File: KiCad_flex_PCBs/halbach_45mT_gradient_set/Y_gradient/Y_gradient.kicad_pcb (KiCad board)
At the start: 2 copper layers, 217.6 x 125.7 mm, 70 parts, among them J1- SolderPad, J2+ SolderPad

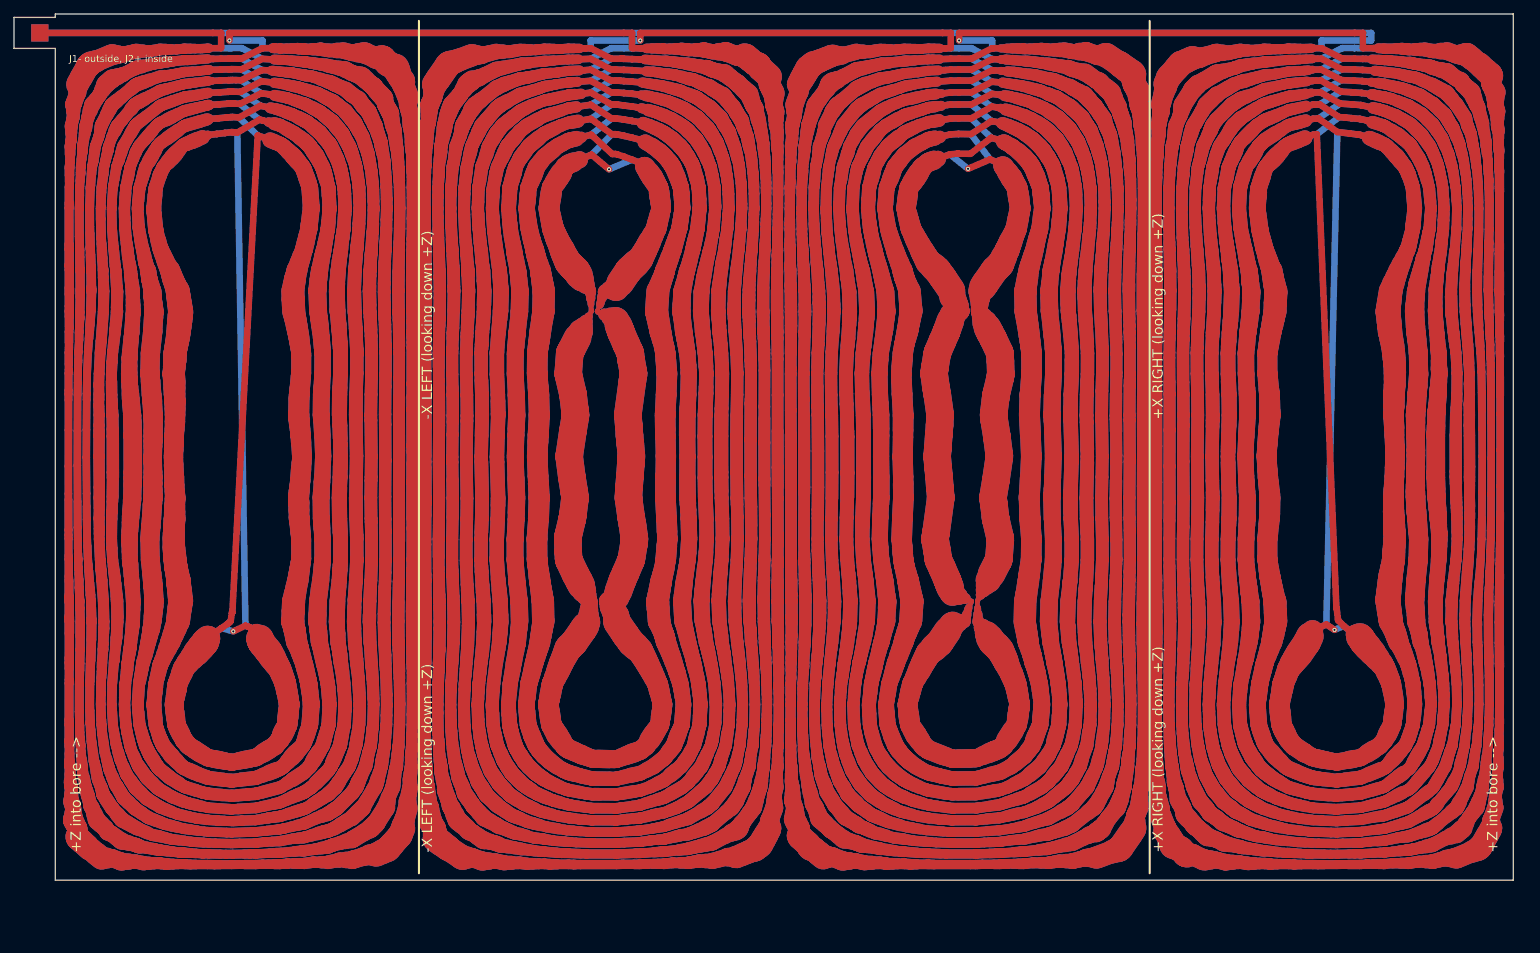
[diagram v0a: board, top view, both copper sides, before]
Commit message: Move the feed tab to the end edge of the flex PCBs
The J1/J2 tab now sticks out past the +axial end of the coil instead of
out of the seam, so the rolled seam is clean and there is room to solder
the leads. Feed and return run as a stacked F.Cu/B.Cu pair along the seam
edge to the routing channel. Larger pads (3 mm) on a 10 mm tab. The tabs
of the three coils sit at their seams: 12, 1 and 6 o'clock looking down +Z.
All boards: DRC clean, same-net gap >= 0.15 mm, re-simulation unchanged.

Co-Authored-By: Claude Opus 5.5 <noreply@anthropic.com>
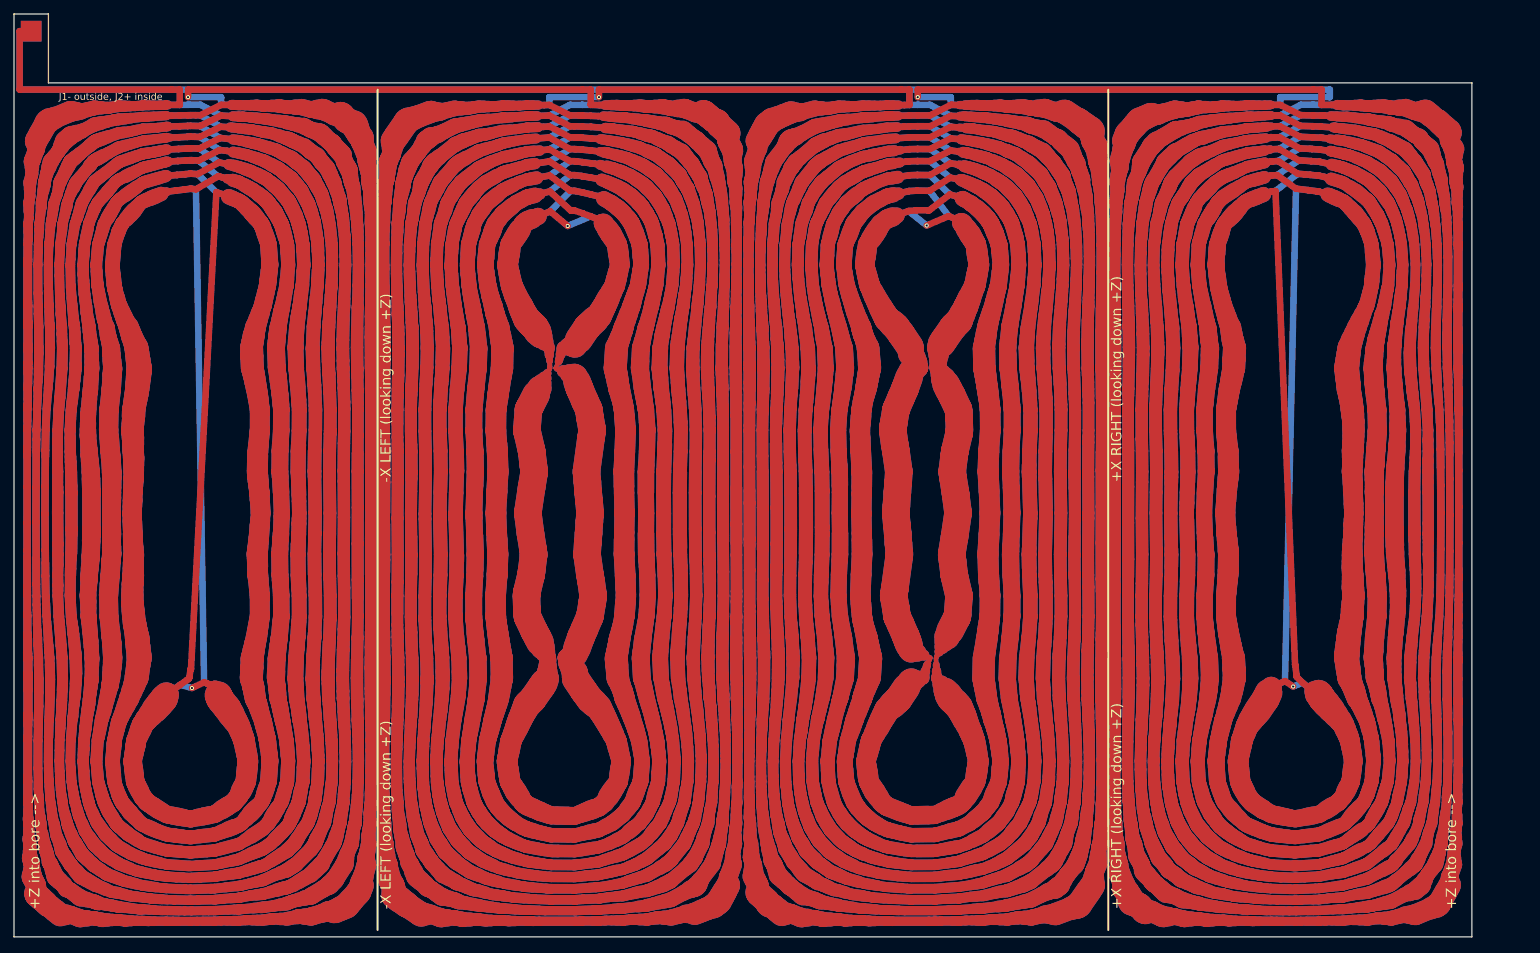
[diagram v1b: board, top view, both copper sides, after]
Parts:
- moved NT9 10.2 mm to (35.1, 106.7)
- moved NT1 10.2 mm to (32.9, 21.0)
- moved NT10 10.2 mm to (34.6, 35.5)
- moved NT13 10.2 mm to (35.1, 29.5)
- moved NT15 10.2 mm to (35.2, 26.3)
- moved NT17 10.2 mm to (35.3, 23.2)
- moved NT18 10.2 mm to (92.5, 21.0)
- moved NT20 10.2 mm to (92.5, 26.3)
- moved NT21 10.2 mm to (92.5, 28.0)
- moved NT22 10.2 mm to (92.5, 29.7)
- moved NT3 10.2 mm to (35.2, 26.3)
- moved NT30 10.2 mm to (92.5, 29.7)
- moved NT31 10.2 mm to (92.5, 28.0)
- moved NT32 10.2 mm to (92.5, 26.3)
- moved NT34 10.2 mm to (92.5, 23.2)
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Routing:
- net G4_B1: track 516.6 -> 523.6 mm
- net COIL_A: track 25.1 -> 32.2 mm
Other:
- board size 217.6 x 125.7 mm -> 211.6 x 133.9 mm

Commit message: Add JLCPCB flex fab profile, stackup, fab checks and board check script
- KiCad_flex_PCBs/fab_profiles/jlcpcb_flex_2layer_1oz_25um_0p2mm.json:
  JLCPCB 2-layer flex (1 oz, 25 um PI, 0.2 mm) stackup, manufacturer
  limits and the design values used.
- export_kicad_flex_pcb 'fab_profile': design values, layer spacing
  (0.06 mm), KiCad stackup (coverlay, Cu, PI, ENIG, 0.2 mm), coverlay
  opening (0.1 mm) and .kicad_pro rules from the profile; every board is
  checked against the limits (report.fab_check).
- check_kicad_flex_pcb / Examples/check_flex_pcb_boards.m: independent
  checks on the board files (KiCad DRC, same-net clearance, manufacturer
  limits, full-width field).
- Boards regenerated: DRC clean, same-net gap >= 0.15 mm, all JLCPCB
  limits met; gradients 7.34 / 19.49 / 18.86 mT/m/A.
- Documentation of the profile and of all checks.

Co-Authored-By: Claude Opus 5.5 <noreply@anthropic.com>
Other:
- rule pad_to_mask_clearance: 0 -> 0.1000
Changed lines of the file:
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@@
 	(generator_version "1.0")
 	(general
-		(thickness 0.11)
+		(thickness 0.2000)
 		(legacy_teardrops no)
 	)
@@
 		(title "Y gradient")
 		(comment 1 "F.Cu is the outside of the rolled cylinder; J1/J2 on the tab past the end of the coil")
-		(comment 2 "CoilGen mapping: x0=11.2500 y0=82.4196 layer_gap=0.1000")
+		(comment 2 "CoilGen mapping: x0=11.2500 y0=82.4196 layer_gap=0.0600")
 	)
 	(layers
@@
 	)
 	(setup
-		(pad_to_mask_clearance 0)
+		(stackup
+			(layer "F.SilkS"
+				(type "Top Silk Screen")
+			)
+			(layer "F.Mask"
+				(type "Top Solder Mask")
+				(color "Yellow")
+				(thickness 0.0500)
+				(material "Polyimide coverlay (PI 25 um + adhesive 25 um)")
+			)
+			(layer "F.Cu"
+				(type "copper")
+				(thickness 0.0350)
+			)
+			(layer "dielectric 1"
+				(type "core")
+				(thickness 0.0250)
+				(material "Polyimide")
+				(epsilon_r 3.5)
+				(loss_tangent 0.002)
+			)
+			(layer "B.Cu"
+				(type "copper")
+				(thickness 0.0350)
+			)
+			(layer "B.Mask"
+				(type "Bottom Solder Mask")
+				(color "Yellow")
+				(thickness 0.0500)
+				(material "Polyimide coverlay (PI 25 um + adhesive 25 um)")
+			)
+			(layer "B.SilkS"
+				(type "Bottom Silk Screen")
+			)
+			(copper_finish "ENIG")
+			(dielectric_constraints no)
+		)
+		(pad_to_mask_clearance 0.1000)
 		(allow_soldermask_bridges_in_footprints no)
 	)

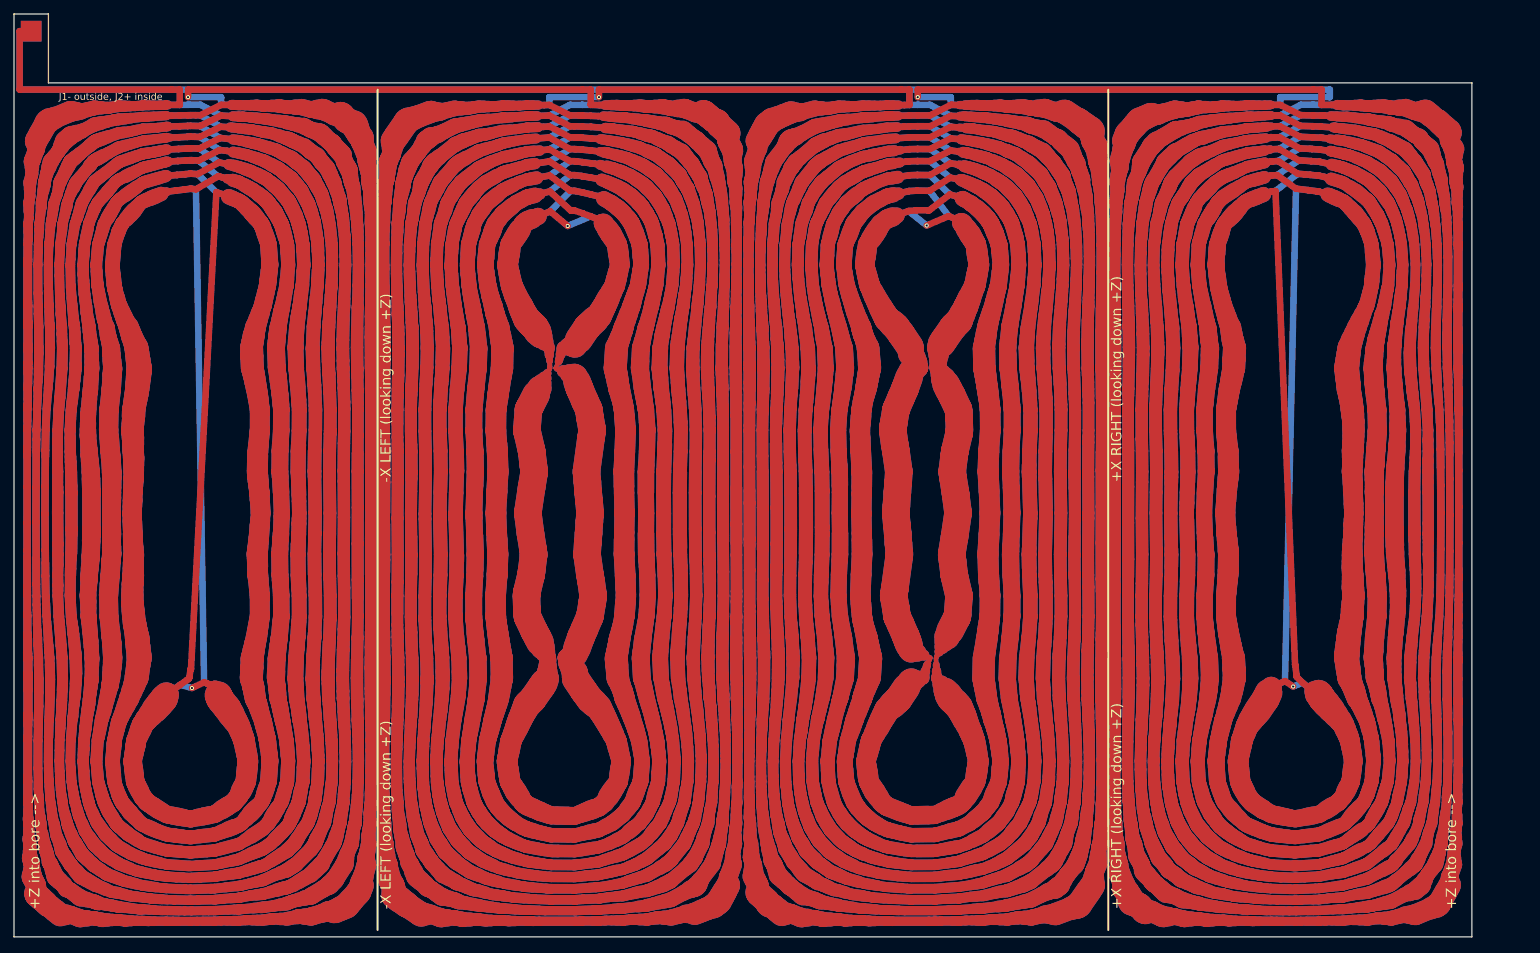
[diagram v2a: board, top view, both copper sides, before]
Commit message: Regenerate the gradient set at 65 / 70 / 75 mm, 120 mm long
- Coils now rolled at 65 (Z), 70 (Y) and 75 mm (X), 120 mm long.
  Z 7.34 mT/m/A, 4.23 ohm, 72 uH, 3.81 A at 28 mT/m (~18.8 V);
  Y 17.9 mT/m/A, 5.05 ohm, 139 uH; X 14.0 mT/m/A, 3.73 ohm, 115 uH.
- All boards: KiCad DRC clean, same-net gap >= 0.15 mm, all JLCPCB
  limits met, re-simulation from the board files matches the design,
  full-width traces change the field by < 0.05 %.
- STEP models and renders regenerated; docs list the tab and seam angles
  and the 24 V check.
- run_kicad_cli: kicad-cli is started with Java's ProcessBuilder and a
  time limit, because MATLAB's system() hangs on macOS after longer
  child processes (STEP export, DRC).

Co-Authored-By: Claude Opus 5.5 <noreply@anthropic.com>
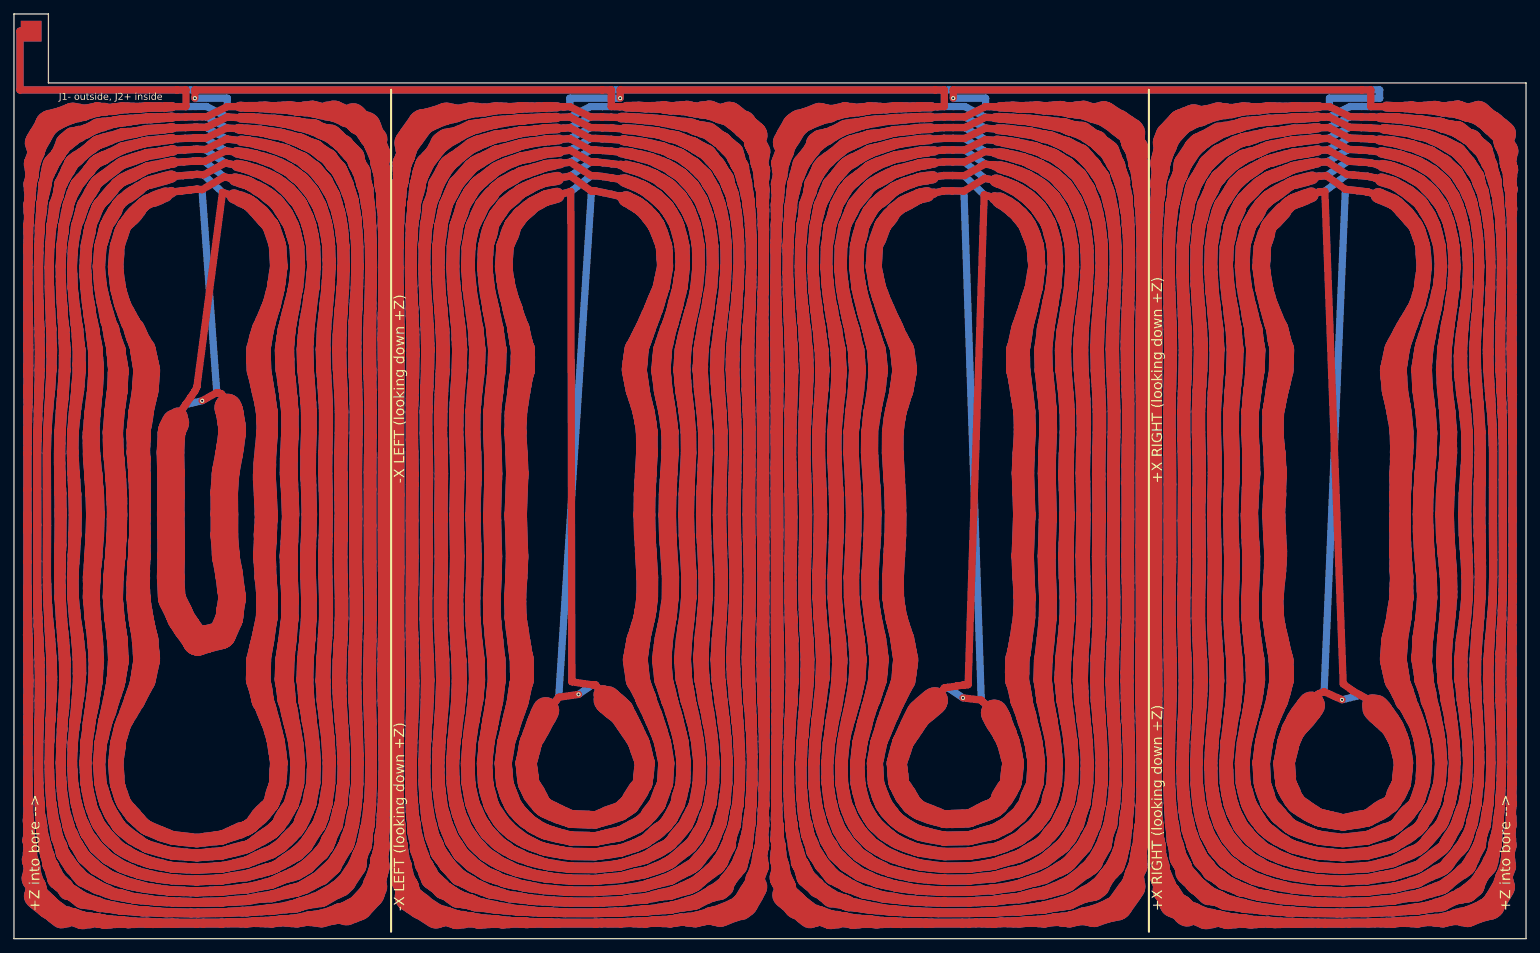
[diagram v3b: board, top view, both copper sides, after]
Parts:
- moved NT43 69.3 mm to (146.8, 107.5)
- moved NT26 68.2 mm to (92.6, 107.2)
- moved NT9 41.1 mm to (35.7, 65.6)
- moved NT60 8.36 mm to (204.3, 108.2)
- moved NT59 7.07 mm to (204.9, 35.6)
- moved NT61 7.07 mm to (204.9, 35.6)
- moved NT58 7.05 mm to (205.1, 33.4)
- moved NT62 7.05 mm to (205.1, 33.4)
- moved NT68 7.04 mm to (205.6, 23.4)
- moved NT52 7.04 mm to (205.6, 21.0)
- moved NT57 7.04 mm to (205.3, 31.5)
- moved NT63 7.04 mm to (205.3, 31.5)
- moved NT54 7.03 mm to (205.5, 26.5)
- moved NT66 7.03 mm to (205.5, 26.5)
- moved NT53 7.03 mm to (205.5, 24.9)
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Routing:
- net G3_T9: track 421.8 -> 182.4 mm
- net G2_T9: track 421.4 -> 184.6 mm
- net G3_T8: track 216.8 -> 286.9 mm
- net G2_T8: track 217.1 -> 286.9 mm
- net G1_T8: track 283.4 -> 245.2 mm
- net G4_B1: track 523.6 -> 534.8 mm
- net G2_B1: track 369.7 -> 375.6 mm
- net G1_B1: track 378.2 -> 383.9 mm
- net G3_B1: track 380.8 -> 386.6 mm
- net G4_T8: track 282.9 -> 288.2 mm
- net G1_T1: track 321.4 -> 325.2 mm
- net G3_T1: track 323.8 -> 327.6 mm
- net G4_T1: track 321.3 -> 325.1 mm
- net G2_T1: track 323.8 -> 327.6 mm
- net G1_T9: track 184.6 -> 188.3 mm
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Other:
- board size 211.6 x 133.9 mm -> 219.4 x 134.2 mm
